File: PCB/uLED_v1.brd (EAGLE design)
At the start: 160 x 100 mm, 17 parts, among them IC1 ATSAMD21E, J2 455-1750-1-ND, SW1 EG1218, U1 AP2112K-3.3

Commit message: Updating board again
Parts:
- removed BT1: (no value), SparkFun-Batteries:BATTCON_12MM_PTH
- added BT2: (no value), SparkFun-Batteries:BATTCON_20MM
- moved C8 15.7 mm to (35.9, 26.0), flipped to the top, turned to 180 degrees
- moved C2 14.9 mm to (35.9, 24.5), flipped to the top, turned to 180 degrees
- moved D1 14.1 mm to (38.6, 22.1), flipped to the top, turned to 180 degrees
- moved U1 13.5 mm to (39.8, 25.4), flipped to the top
- moved C1 10.6 mm to (54.2, 14.5), flipped to the top, turned to 0 degrees
- moved LED1 9.60 mm to (53.3, 25.1), turned to 180 degrees
- moved SW1 9.16 mm to (55.2, 19.1), turned to 270 degrees
- moved J1 7.82 mm to (52.7, 36.2)
- moved R2 7.51 mm to (48.4, 31.2)
- moved R3 7.39 mm to (45.1, 31.2)
- moved R1 7.15 mm to (51.7, 31.2)
- moved CTRL 6.63 mm to (43.8, 23.4), turned to 270 degrees
- moved C3 6.25 mm to (47.1, 18.0)
- moved IC1 6.00 mm to (48.9, 24.1)
- moved J2 5.73 mm to (46.2, 12.7)
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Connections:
- new net LEDCI: IC1.7, LED1.5
- new net LEDDI: IC1.8, LED1.6
- net ANODE: now also IC1.14; no longer IC1.8
- net GND: now also BT2.2; no longer BT1.GND
- net VBAT: now also BT2.1; no longer BT1.VCC@1
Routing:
- net 3.3V: track 20.3 -> 47.4 mm, vias 1 -> 3
- net VOUT: track 7.57 -> 33.7 mm, vias 1 -> 2
- net GND: track 23.3 -> 2.75 mm, vias 3 -> 0
- net VHIGH: track 6.53 -> 15.2 mm, vias 1 -> 2
- net ANODE: track 4.54 -> 11.9 mm
- net REDOUT: track 1.74 -> 6.42 mm
- net N$2: track 3.19 -> 5.80 mm
- net N$3: track 2.64 -> 5.04 mm
- net VDDCORE: track 1.86 -> 4.26 mm
- net VBAT: track 4.56 -> 2.50 mm, vias 0 -> 1
- net GREENOUT: track 2.62 -> 4.65 mm
- net BLUEOUT: track 5.29 -> 7.32 mm
- net SWCLK: track 12.3 -> 10.3 mm
- net N$1: track 3.21 -> 5.12 mm
- net LEDCI: track 0.00 -> 1.23 mm
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
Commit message: yet another pcb
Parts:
- removed BT2: (no value), SparkFun-Batteries:BATTCON_20MM
- added U$3: 20MM_BATTERY, mikes:BATTCON_20MM
- moved C2 21.3 mm to (55.6, 32.6), turned to 90 degrees
- moved C8 19.3 mm to (54.1, 32.5), turned to 90 degrees
- moved D1 19.2 mm to (57.7, 24.6)
- moved U1 18.0 mm to (57.5, 27.9)
- moved C1 17.5 mm to (57.8, 31.6), turned to 90 degrees
- moved SW1 0.64 mm to (55.9, 19.1)
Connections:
- new net +1: U$3.1
- net GND: now also U$3.2; no longer BT2.2
- net VBAT: now also U$3.3; no longer BT2.1
- net VHIGH: now also SW1.O1; no longer SW1.O2
- net VOUT: now also SW1.P1; no longer SW1.P2
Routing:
- net VOUT: track 33.7 -> 22.8 mm, vias 2 -> 0
- net VHIGH: track 15.2 -> 4.75 mm, vias 2 -> 0
- net VBAT: track 2.50 -> 7.56 mm
- net GND: track 2.75 -> 5.77 mm
- net 3.3V: track 47.4 -> 45.8 mm

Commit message: PCB version 1 final
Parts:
- moved C3 0.90 mm to (48.0, 17.9), turned to 270 degrees
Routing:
- net 3.3V: track 45.8 -> 33.1 mm
- net VDDCORE: track 4.26 -> 3.34 mm
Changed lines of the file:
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@@
 <layer number="20" name="Dimension" color="24" fill="1" visible="yes" active="yes"/>
 <layer number="21" name="tPlace" color="7" fill="1" visible="yes" active="yes"/>
-<layer number="22" name="bPlace" color="7" fill="1" visible="no" active="yes"/>
+<layer number="22" name="bPlace" color="7" fill="1" visible="yes" active="yes"/>
 <layer number="23" name="tOrigins" color="15" fill="1" visible="yes" active="yes"/>
-<layer number="24" name="bOrigins" color="15" fill="1" visible="no" active="yes"/>
+<layer number="24" name="bOrigins" color="15" fill="1" visible="yes" active="yes"/>
 <layer number="25" name="tNames" color="7" fill="1" visible="yes" active="yes"/>
-<layer number="26" name="bNames" color="7" fill="1" visible="no" active="yes"/>
-<layer number="27" name="tValues" color="7" fill="1" visible="yes" active="yes"/>
+<layer number="26" name="bNames" color="7" fill="1" visible="yes" active="yes"/>
+<layer number="27" name="tValues" color="7" fill="1" visible="no" active="yes"/>
 <layer number="28" name="bValues" color="7" fill="1" visible="no" active="yes"/>
 <layer number="29" name="tStop" color="7" fill="3" visible="no" active="yes"/>
@@
 <layer number="38" name="bTest" color="7" fill="1" visible="no" active="yes"/>
 <layer number="39" name="tKeepout" color="4" fill="11" visible="yes" active="yes"/>
-<layer number="40" name="bKeepout" color="1" fill="11" visible="no" active="yes"/>
+<layer number="40" name="bKeepout" color="1" fill="11" visible="yes" active="yes"/>
 <layer number="41" name="tRestrict" color="4" fill="10" visible="yes" active="yes"/>
-<layer number="42" name="bRestrict" color="1" fill="10" visible="no" active="yes"/>
+<layer number="42" name="bRestrict" color="1" fill="10" visible="yes" active="yes"/>
 <layer number="43" name="vRestrict" color="2" fill="10" visible="no" active="yes"/>
 <layer number="44" name="Drills" color="7" fill="1" visible="no" active="yes"/>
@@
 <layer number="50" name="dxf" color="7" fill="1" visible="no" active="no"/>
 <layer number="51" name="tDocu" color="7" fill="1" visible="yes" active="yes"/>
-<layer number="52" name="bDocu" color="7" fill="1" visible="no" active="yes"/>
+<layer number="52" name="bDocu" color="7" fill="1" visible="yes" active="yes"/>
 <layer number="53" name="tGND_GNDA" color="7" fill="9" visible="no" active="no"/>
 <layer number="54" name="bGND_GNDA" color="1" fill="9" visible="no" active="no"/>
@@
 </autorouter>
 <elements>
-<element name="C3" library="microbuilder" package="0603-NO" value="1uF" x="47.117" y="18.034" rot="R180">
-<attribute name="NAME" x="45.339" y="18.161" size="0.8128" layer="25" font="vector" ratio="18" rot="R180"/>
-<attribute name="VALUE" x="45.339" y="18.796" size="0.4064" layer="27" font="vector" ratio="10" rot="R180"/>
+<element name="C3" library="microbuilder" package="0603-NO" value="1uF" x="48.006" y="17.907" rot="R270">
+<attribute name="NAME" x="47.879" y="16.129" size="0.8128" layer="25" font="vector" ratio="18" rot="R270"/>
+<attribute name="VALUE" x="47.244" y="16.129" size="0.4064" layer="27" font="vector" ratio="10" rot="R270"/>
 </element>
 <element name="IC1" library="microbuilder" package="QFN32_5MM" value="ATSAMD21E" x="48.895" y="24.13" rot="R180"/>
@@
 <contactref element="IC1" pad="29"/>
 <wire x1="49.145" y1="20.32" x2="49.145" y2="21.63" width="0.3048" layer="1"/>
-<wire x1="47.967" y1="18.034" x2="48.26" y2="18.034" width="0.3048" layer="1"/>
-<wire x1="48.26" y1="19.435" x2="49.145" y2="20.32" width="0.3048" layer="1"/>
-<wire x1="48.26" y1="18.034" x2="48.26" y2="19.435" width="0.3048" layer="1"/>
+<wire x1="49.145" y1="20.32" x2="48.26" y2="19.435" width="0.3048" layer="1"/>
+<wire x1="48.26" y1="19.435" x2="48.26" y2="19.011" width="0.1524" layer="1"/>
+<wire x1="48.26" y1="19.011" x2="48.006" y2="18.757" width="0.1524" layer="1"/>
 </signal>
 <signal name="ANODE">
@@
 <contactref element="IC1" pad="9"/>
 <contactref element="LED1" pad="3"/>
-<wire x1="39.37" y1="27.94" x2="52.07" y2="27.94" width="0.508" layer="16"/>
 <via x="52.07" y="27.94" extent="1-16" drill="0.35"/>
 <wire x1="54.29" y1="24.384" x2="54.29" y2="24.396" width="0.3048" layer="1"/>

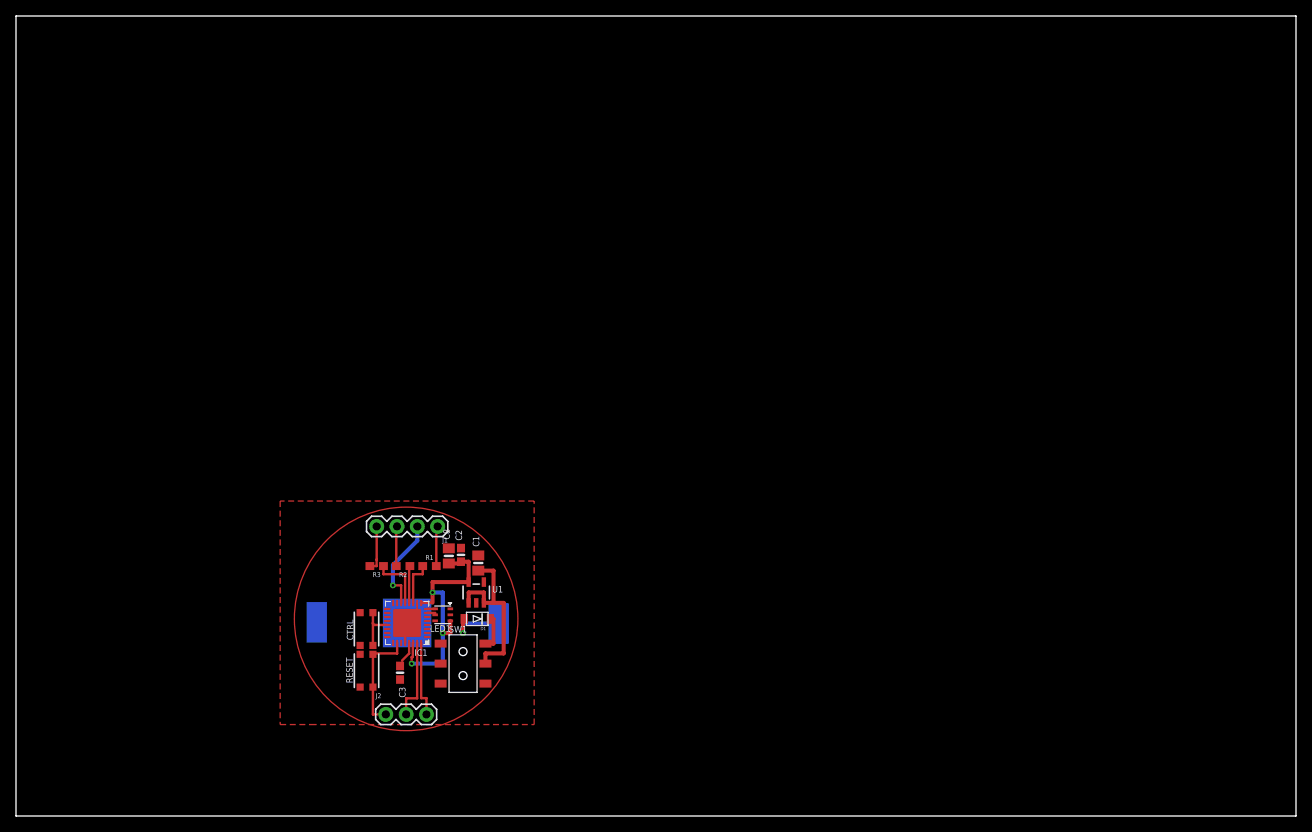
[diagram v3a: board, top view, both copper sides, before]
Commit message: adding UART4Debugging
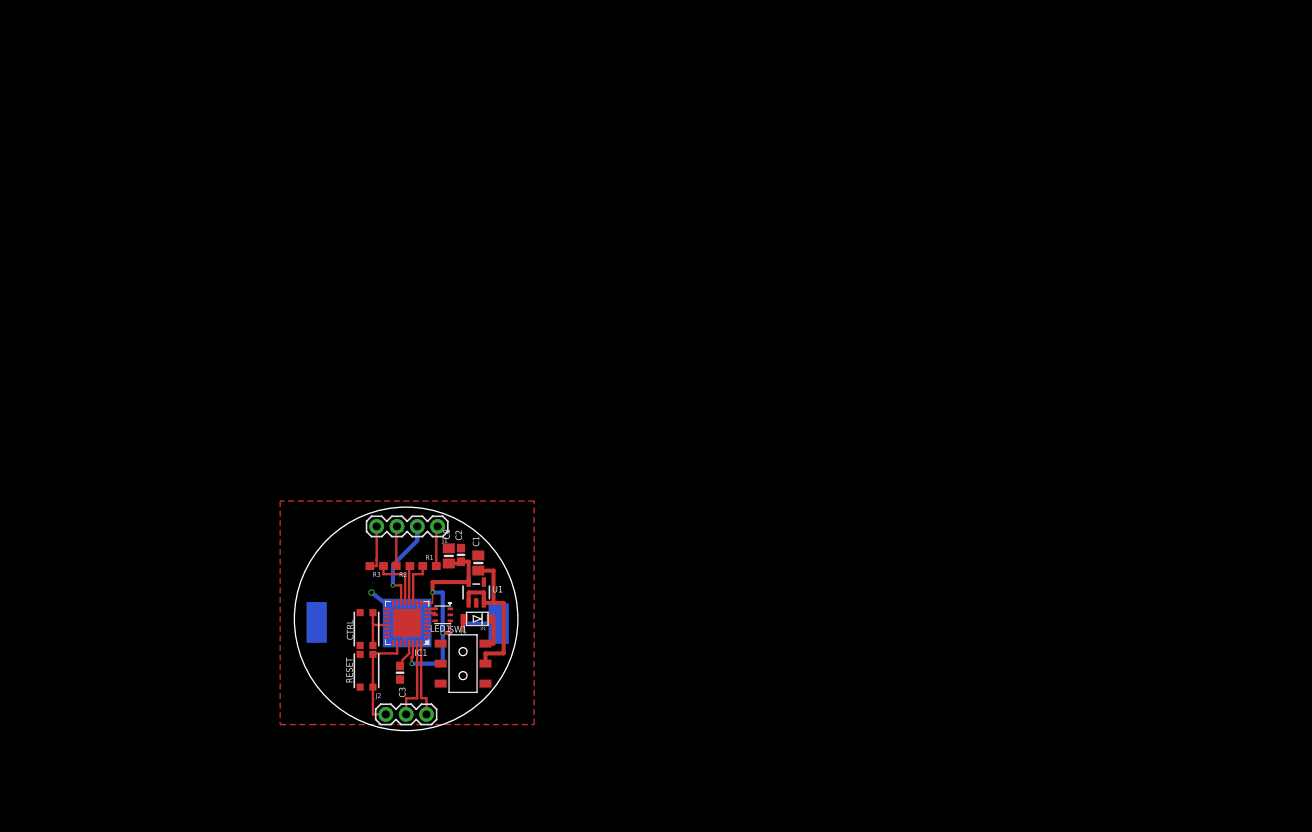
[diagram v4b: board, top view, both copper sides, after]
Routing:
- net GND: track 5.77 -> 11.5 mm, vias 0 -> 1
- net REDOUT: track 6.42 -> 5.81 mm
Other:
- board size 160 x 100 mm -> 27.9 x 27.9 mm

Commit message: Saturday Morning Commit
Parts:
- removed RESET: (no value), microbuilder:BTN_KMR2_4.6X2.8
- removed SW1: EG1218, microbuilder:EG1390
- removed U$3: 20MM_BATTERY, mikes:BATTCON_20MM
- added BT1: (no value), SparkFun-Batteries:BATTCON_12MM
- added J3, J4, J5, J6: (no value), SparkFun-Connectors:1X01
- J2: value 455-1750-1-ND -> (none); device SparkFun-Connectors:1X03 -> SparkFun-Connectors:1X01
- moved J2 15.9 mm to (40.6, 27.6)
- moved D1 10.3 mm to (51.7, 16.3), turned to 210 degrees
- moved C2 10.2 mm to (56.9, 22.5)
- moved R3 9.61 mm to (54.4, 28.7)
- moved J1 9.56 mm to (44.5, 31.4), turned to 0 degrees
- moved C1 9.20 mm to (54.6, 23.0), turned to 180 degrees
- moved U1 8.92 mm to (53.3, 20.1), turned to 180 degrees
- moved R1 7.50 mm to (45.0, 27.9), turned to 90 degrees
- moved C8 6.59 mm to (55.9, 26.2), turned to 270 degrees
- moved R2 2.98 mm to (50.7, 29.3)
- moved C3 2.73 mm to (45.6, 19.2), turned to 180 degrees
- moved CTRL 2.54 mm to (41.3, 23.4)
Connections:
- net N$2 renamed BLUELED
- net N$3 renamed GREENLED
- removed net +1: U$3.1
- removed net N$1: J1.1, R1.2
- removed net SERCOM_1+3.0: IC1.17
- removed net SERCOM_1+3.1: IC1.18
- removed net VOUT: C1.1, SW1.P1, U1.1, U1.3
- new net REDLED: IC1.16, J1.1, R1.2
- net 3.3V: now also J6.1
- net GND: now also BT1.GND, J2.1; no longer RESET.B, RESET.B', U$3.2
- net RESETN: now also J3.1; no longer J2.1, RESET.A, RESET.A'
- net SCDIO: now also J5.1; no longer J2.3
- net SWCLK: now also J4.1; no longer J2.2
- net VBAT: now also BT1.PWR@1; no longer U$3.3
- net VHIGH: now also C1.1, U1.1, U1.3; no longer SW1.O1
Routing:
- net VOUT: track 22.8 -> 0.00 mm
- net 3.3V: track 33.1 -> 42.6 mm
- net REDOUT: track 5.81 -> 14.3 mm, vias 0 -> 2
- net REDLED: track 0.00 -> 7.14 mm
- net ANODE: track 11.9 -> 5.22 mm, vias 1 -> 0
- net BUTTON: track 5.98 -> 12.5 mm
- net VBAT: track 7.56 -> 12.9 mm
- net N$1: track 5.12 -> 0.00 mm
- net VHIGH: track 4.49 -> 9.46 mm
- net RESETN: track 13.6 -> 10.5 mm, vias 0 -> 1
- net BLUEOUT: track 7.32 -> 10.3 mm, vias 0 -> 2
- net GREENLED: track 5.04 -> 2.19 mm
- net BLUELED: track 5.80 -> 3.08 mm
- net VDDCORE: track 3.34 -> 5.05 mm, vias 0 -> 1
- net GND: track 11.5 -> 12.8 mm, vias 1 -> 2
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- added copper zone on layer 16, net GND
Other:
- board size 27.9 x 27.9 mm -> 20.3 x 20.3 mm

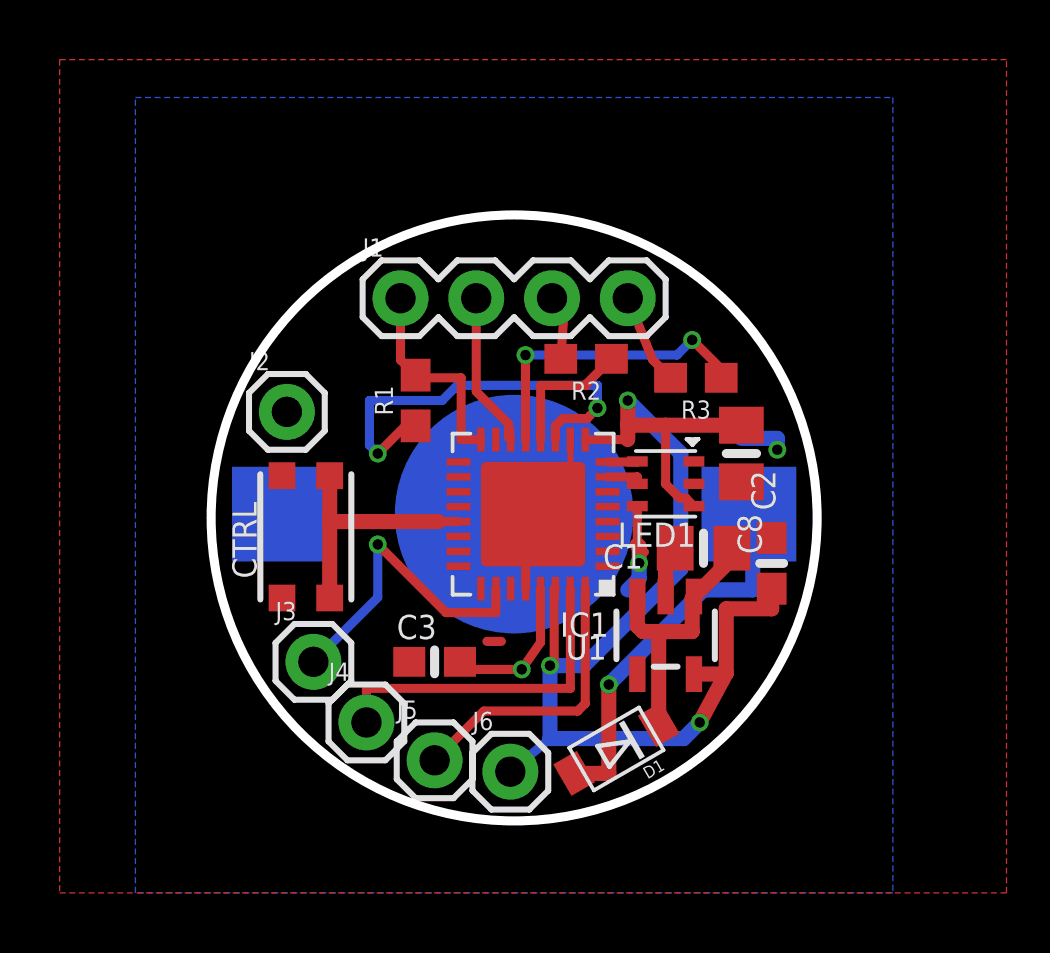
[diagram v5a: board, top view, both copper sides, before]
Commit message: Adding new PCB 16mm
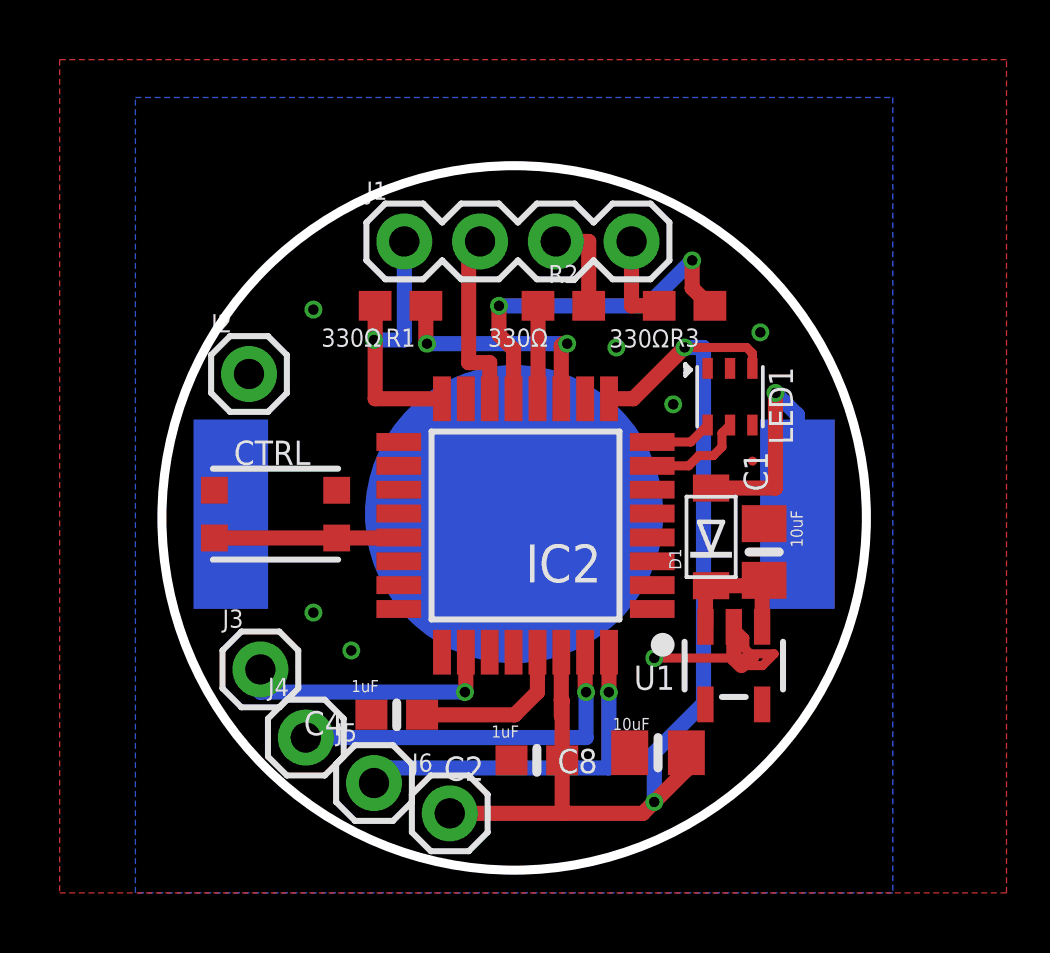
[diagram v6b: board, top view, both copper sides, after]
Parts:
- removed C3: 1uF, microbuilder:0603-NO
- removed IC1: ATSAMD21E, microbuilder:QFN32_5MM
- added C4: 1uF, microbuilder:0603-NO
- added IC2: ATSAMD21E18A-AFT, SamacSys_Parts:QFP80P900X900X120-32N
- moved C8 10.4 mm to (53.1, 16.1), turned to 180 degrees
- moved C2 10.3 mm to (49.0, 15.9), turned to 180 degrees
- moved D1 7.79 mm to (54.9, 23.4), turned to 90 degrees
- moved LED1 3.63 mm to (55.5, 28.1), turned to 270 degrees
- moved R1 3.22 mm to (44.5, 31.1), turned to 180 degrees
- moved U1 2.50 mm to (55.6, 19.1)
- moved J6 2.47 mm to (46.1, 14.1)
- moved R3 2.44 mm to (54.0, 31.1)
- moved J5 2.17 mm to (43.6, 15.1)
- moved J4 2.09 mm to (41.3, 16.6)
- moved C1 2.04 mm to (56.6, 22.9), turned to 90 degrees
- moved R2 1.93 mm to (49.9, 31.1), turned to 0 degrees
- moved J1 1.91 mm to (44.6, 33.3)
- moved J3 1.80 mm to (39.8, 18.9)
- moved J2 1.80 mm to (39.4, 28.8)
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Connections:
- removed net D3: IC1.1
- net 3.3V: now also IC2.30, IC2.9; no longer IC1.30, IC1.9
- net ANODE: now also IC2.14; no longer IC1.14
- net BLUEOUT: now also IC2.13; no longer IC1.13
- net BUTTON: now also IC2.21; no longer IC1.21
- net GND: now also C4.2, IC2.10, IC2.28; no longer C3.2, IC1.10, IC1.28, IC1.33
- net GREENOUT: now also IC2.12; no longer IC1.12
- net LEDCI: now also IC2.7; no longer IC1.7
- net LEDDI: now also IC2.8; no longer IC1.8
- net REDLED: now also IC2.16; no longer IC1.16
- net REDOUT: now also IC2.11; no longer IC1.11
- net RESETN: now also IC2.26; no longer IC1.26
- net SCDIO: now also IC2.32; no longer IC1.32
- net SWCLK: now also IC2.31; no longer IC1.31
- net VDDCORE: now also C4.1, IC2.29; no longer C3.1, IC1.29
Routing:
- net BUTTON: track 12.5 -> 6.19 mm
- net REDOUT: track 14.3 -> 8.01 mm
- net 3.3V: track 42.6 -> 37.8 mm, vias 3 -> 2
- net GND: track 12.8 -> 8.17 mm, vias 2 -> 7
- net VHIGH: track 9.46 -> 6.14 mm
- net VBAT: track 12.9 -> 9.72 mm
- net REDLED: track 7.14 -> 9.73 mm, vias 0 -> 1
- net SCDIO: track 9.69 -> 12.0 mm, vias 0 -> 1
- net LEDCI: track 1.23 -> 3.45 mm
- net BLUEOUT: track 10.3 -> 12.2 mm
- net RESETN: track 10.5 -> 8.99 mm
- net GREENOUT: track 4.58 -> 3.14 mm
- net ANODE: track 5.22 -> 6.36 mm
- net LEDDI: track 1.01 -> 2.09 mm
- net GREENLED: track 2.19 -> 3.26 mm
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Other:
- board size 20.3 x 20.3 mm -> 23.6 x 23.6 mm
